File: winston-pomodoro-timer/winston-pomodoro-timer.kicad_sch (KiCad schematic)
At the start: 33 parts, among them J1 Conn_01x05_Pin, J2 Conn_01x05_Pin, J4 Conn_01x04_Pin, J5 Conn_01x06_Pin, U1 ATmega328P-A, Y1 Crystal_GND24

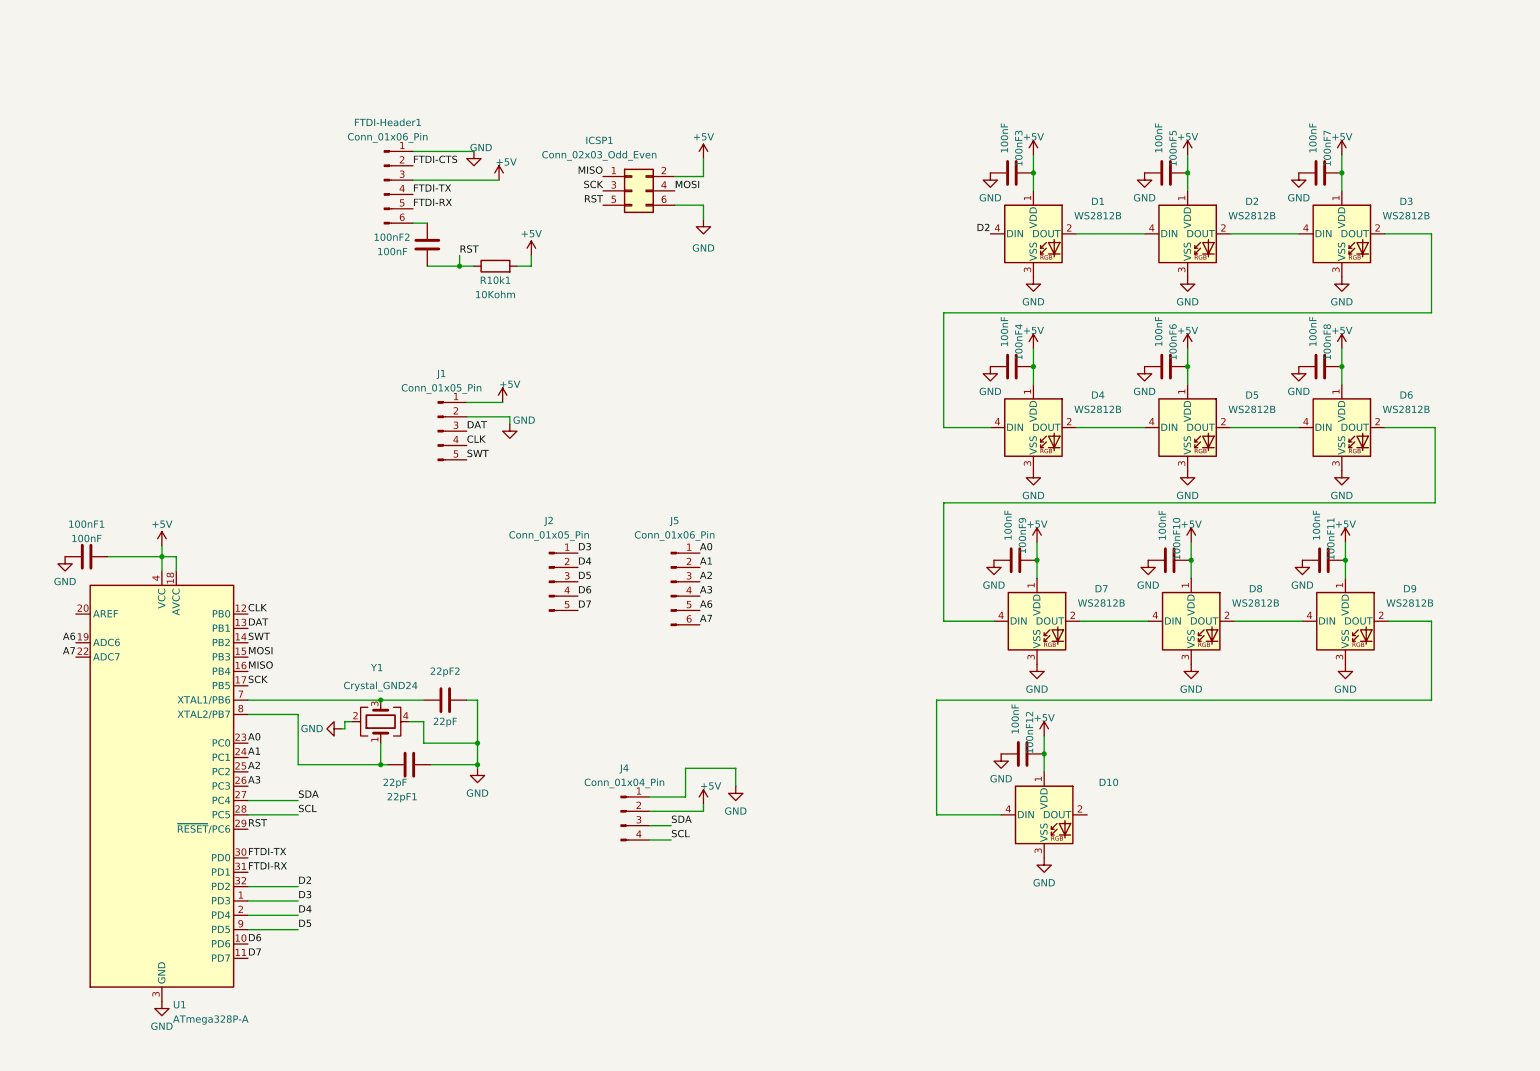
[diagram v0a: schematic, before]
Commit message: added usbc port and started battery controller
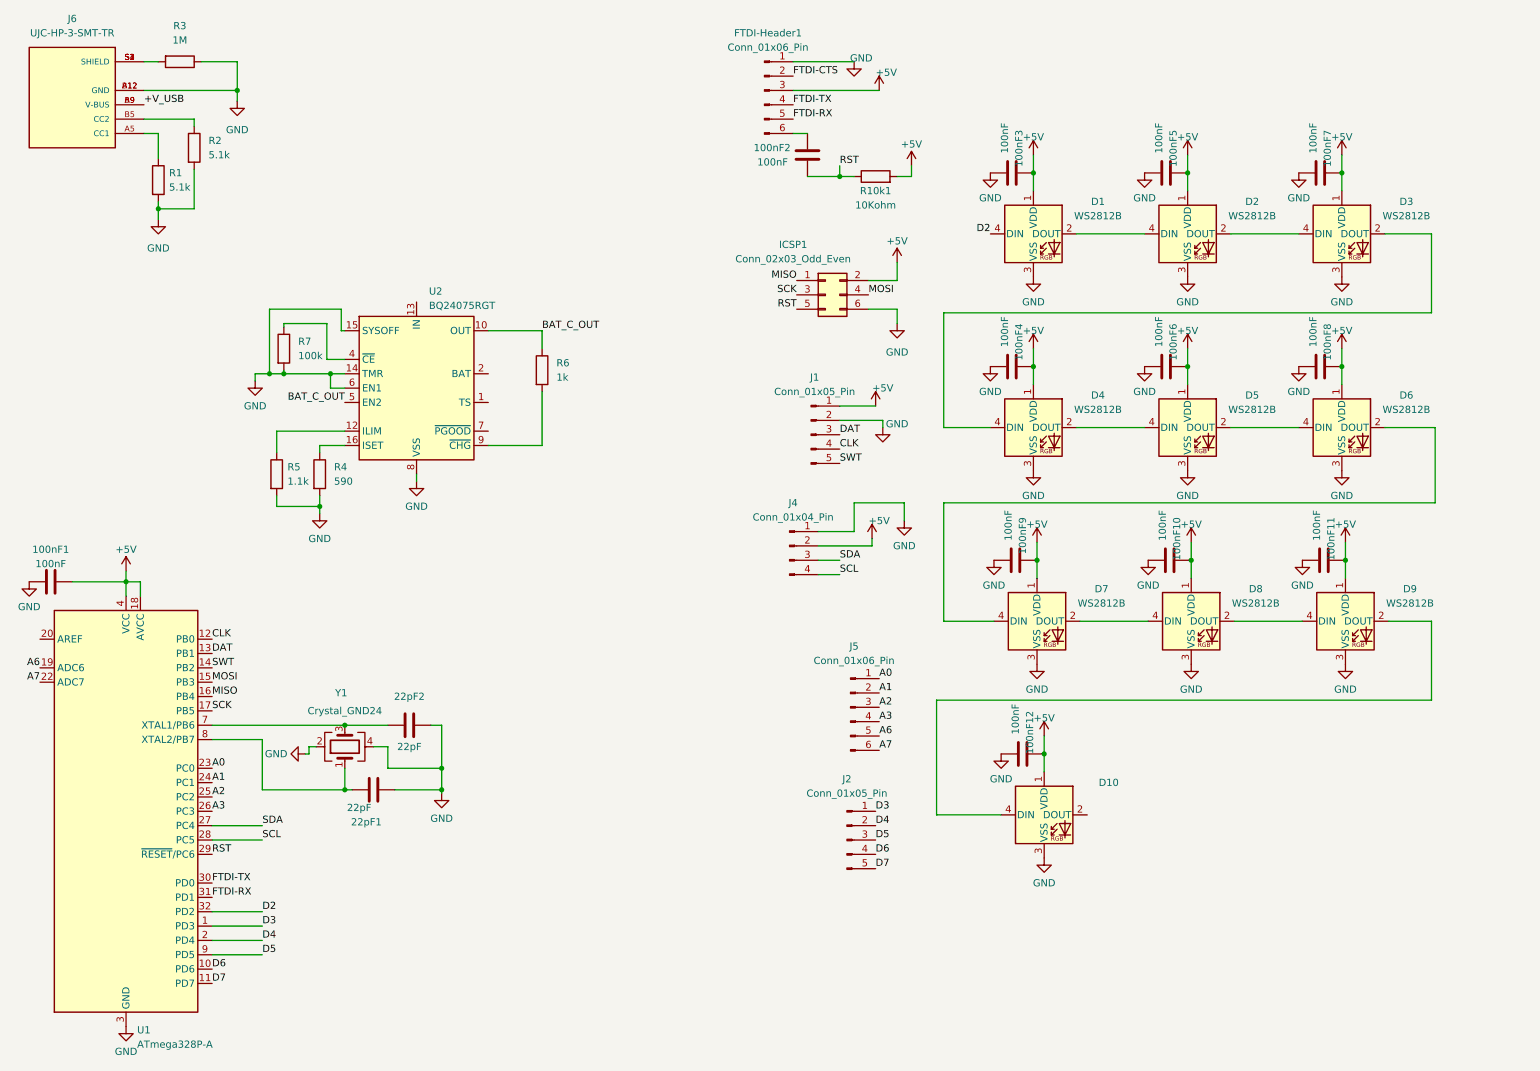
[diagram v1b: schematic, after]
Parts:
- added J6: UJC-HP-3-SMT-TR, UJC-HP-3-SMT-TR:CUI_UJC-HP-3-SMT-TR, symbol UJC-HP-3-SMT-TR:UJC-HP-3-SMT-TR
- added R1, R2: 5.1k, symbol Device:R
- added R3: 1M, symbol Device:R
- added R4: 590, symbol Device:R
- added R5: 1.1k, symbol Device:R
- added R6: 1k, symbol Device:R
- added R7: 100k, symbol Device:R
- added U2: BQ24075RGT, Package_DFN_QFN:VQFN-16-1EP_3x3mm_P0.5mm_EP1.6x1.6mm, symbol Battery_Management:BQ24075RGT
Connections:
- net GND: now also J6.A12 (GND), J6.B12 (GND), R1.2, R2.2, R3.1, R4.2, R5.2, R7.2, U2.14 (TMR), U2.15 (SYSOFF), U2.17 (VSS), U2.6 (EN1), U2.8 (VSS)
- new net: J6.S1 (SHIELD), J6.S2 (SHIELD), J6.S3 (SHIELD), J6.S4 (SHIELD), R3.2
- new net: R5.1, U2.12 (ILIM)
- new net: R4.1, U2.16 (ISET)
- new net: U2.2 (BAT), U2.3 (BAT)
- new net: R7.1, U2.4 (~{CE})
- new net: R6.2, U2.9 (~{CHG})
- new net: J6.A5 (CC1), R1.1
- new net: J6.B5 (CC2), R2.1
- new net +V_USB: J6.A9 (V-BUS), J6.B9 (V-BUS)
- new net BAT_C_OUT: R6.1, U2.10 (OUT), U2.11 (OUT), U2.5 (EN2)
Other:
- moved on the sheet: 100nF1, 100nF2, 22pF1, 22pF2, FTDI-Header1, ICSP1, J1, J2, J4, J5, R10k1, U1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

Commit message: finished layout and routing
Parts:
- added C1, C2: 10uF, Capacitor_SMD:C_0603_1608Metric, symbol Device:C
- added C3: 100uF, Capacitor_SMD:C_0805_2012Metric, symbol Device:C
- added C4: 22uF, Capacitor_SMD:C_0603_1608Metric, symbol Device:C
- added J3: Battery_Conn, Connector_PinSocket_2.00mm:PinSocket_1x02_P2.00mm_Vertical, symbol Connector:Conn_01x02_Pin
- added L1: 6.8uH, Inductor_SMD:L_Bourns-SRN4018, symbol Device:L
- added R10: 2.2M, Resistor_SMD:R_0603_1608Metric, symbol Device:R
- added R11: 390K, Resistor_SMD:R_0603_1608Metric, symbol Device:R
- added R12: 1.8M, Capacitor_SMD:C_0603_1608Metric, symbol Device:R
- added R13, R9: 200K, Resistor_SMD:R_0603_1608Metric, symbol Device:R
- added R8: 10k, Resistor_SMD:R_0603_1608Metric, symbol Device:R
- added SW2: SW_SPDT, Button_Switch_THT:SW_Slide_1P2T_CK_OS102011MS2Q, symbol Switch:SW_SPDT
- added U3: TPS61092RSAR, TPS61092RSAR:CONV_TPS61092RSAR, symbol TPS61092RSAR:TPS61092RSAR
- 100nF1, 100nF10, 100nF11, 100nF12, 100nF2, 100nF3, 100nF4, 100nF5, 100nF6, 100nF7, 100nF8, 100nF9, 22pF1, 22pF2: footprint Capacitor_SMD:C_0805_2012Metric_Pad1.18x1.45mm_HandSolder -> Capacitor_SMD:C_0603_1608Metric
- R1, R2, R3, R4, R5, R6, R7: footprint (none) -> Resistor_SMD:R_0603_1608Metric
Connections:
- net +5V: now also C3.1, R12.1, U3.1 (VOUT), U3.15 (VOUT), U3.16 (VOUT)
- net +V_USB: now also U2.13 (IN), C4.1
- net GND: now also C1.2, C2.2, C3.2, C4.2, J3.2 (Pin_2), R11.2, R13.2, R8.2, SW2.3 (C), U3.10 (SYNC), U3.12 (LBO), U3.13 (GND), U3.17 (PGND), U3.5 (PGND), U3.6 (PGND), U3.7 (PGND)
- net at U2.1 (TS): now also R8.1
- net +V_BAT: now reaches U2.2 (BAT), U2.3 (BAT)
- net +V_BAT: now also C1.1, J3.1 (Pin_1)
- net BAT_C_OUT renamed BAT_V_OUT
- net BAT_V_OUT: now also C2.1, L1.1, R10.1, SW2.1 (A), U3.8 (VBAT)
- new net: R10.2, R11.1, U3.9 (LBI)
- new net: R13.1, R9.2, U3.14 (FB)
- new net: L1.2, U3.3 (SW), U3.4 (SW)
- new net: R12.2, R9.1
- new net Boost_EN: SW2.2 (B), U3.11 (EN)
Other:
- note added: "Enable Boost"
- note added: "Power Switch"
- note added: "R10 and R11 disconnect the battery from the system when it drops below 3.35v >>Check voltage range of Winston's battery"
- note added: "Shutdown Boost"
- moved on the sheet: 22pF1, 22pF2, J2, J4, J5, R1, R2, R4, R5, R6, R7, U2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

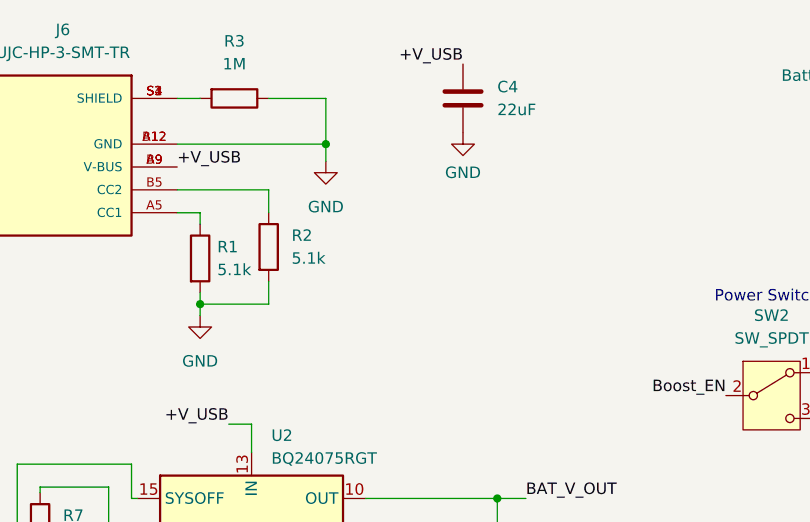
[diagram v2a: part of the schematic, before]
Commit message: added battery override jumpers
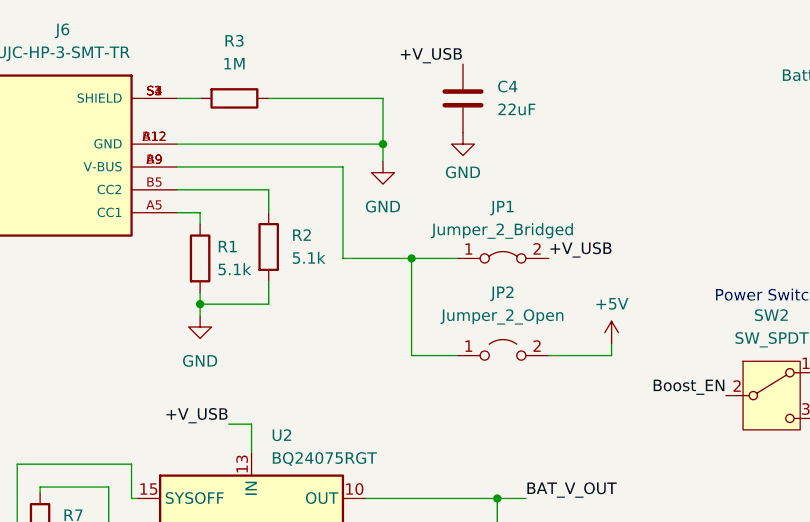
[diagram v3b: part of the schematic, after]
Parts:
- added JP1: Jumper_2_Bridged, Jumper:SolderJumper-2_P1.3mm_Bridged2Bar_RoundedPad1.0x1.5mm, symbol Jumper:Jumper_2_Bridged
- added JP2: Jumper_2_Open, Jumper:SolderJumper-2_P1.3mm_Open_RoundedPad1.0x1.5mm, symbol Jumper:Jumper_2_Open
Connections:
- net +5V: now also JP2.2 (B)
- net +V_USB: now also JP1.2 (B); no longer J6.A9 (V-BUS), J6.B9 (V-BUS)
- new net: J6.A9 (V-BUS), J6.B9 (V-BUS), JP1.1 (A), JP2.1 (A)
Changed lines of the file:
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@@
   (junction (at 19.685 74.295) (diameter 0) (color 0 0 0 0)
   )
+  (junction (at 60.96 40.005) (diameter 0) (color 0 0 0 0)
+  )
   (junction (at 17.145 74.295) (diameter 0) (color 0 0 0 0)
   )
+  (junction (at 57.785 27.305) (diameter 0) (color 0 0 0 0)
+  )
   (junction (at 247.015 41.91) (diameter 0) (color 0 0 0 0)
   )
@@
   (junction (at 194.31 144.78) (diameter 0) (color 0 0 0 0)
   )
-  (junction (at 51.435 27.305) (diameter 0) (color 0 0 0 0)
-  )
   (junction (at 153.67 171.45) (diameter 0) (color 0 0 0 0)
   )
@@
     (stroke (width 0) (type default))
   )
-  (wire (pts (xy 34.925 27.305) (xy 51.435 27.305))
+  (wire (pts (xy 34.925 27.305) (xy 57.785 27.305))
     (stroke (width 0) (type default))
   )
@@
     (stroke (width 0) (type default))
   )
-  (wire (pts (xy 51.435 27.305) (xy 51.435 29.21))
+  (wire (pts (xy 57.785 27.305) (xy 57.785 29.21))
     (stroke (width 0) (type default))
   )
@@
     (stroke (width 0) (type default))
   )
+  (wire (pts (xy 83.185 50.8) (xy 83.185 49.53))
+    (stroke (width 0) (type default))
+  )
   (wire (pts (xy 193.04 110.49) (xy 193.04 113.665))
     (stroke (width 0) (type default))
@@
     (stroke (width 0) (type default))
   )
+  (wire (pts (xy 53.34 29.845) (xy 53.34 40.005))
+    (stroke (width 0) (type default))
+  )
   (wire (pts (xy 162.56 181.61) (xy 162.56 182.88))
     (stroke (width 0) (type default))
@@
     (stroke (width 0) (type default))
   )
+  (wire (pts (xy 60.96 40.005) (xy 66.04 40.005))
+    (stroke (width 0) (type default))
+  )
   (wire (pts (xy 27.94 74.295) (xy 30.48 74.295))
     (stroke (width 0) (type default))
@@
     (stroke (width 0) (type default))
   )
-  (wire (pts (xy 51.435 22.225) (xy 51.435 27.305))
+  (wire (pts (xy 57.785 22.225) (xy 57.785 27.305))
     (stroke (width 0) (type default))
   )
@@
     (stroke (width 0) (type default))
   )
+  (wire (pts (xy 76.2 50.8) (xy 83.185 50.8))
+    (stroke (width 0) (type default))
+  )
   (wire (pts (xy 255.27 121.285) (xy 262.89 121.285))
     (stroke (width 0) (type default))
@@
     (stroke (width 0) (type default))
   )
-  (wire (pts (xy 45.085 22.225) (xy 51.435 22.225))
+  (wire (pts (xy 45.085 22.225) (xy 57.785 22.225))
     (stroke (width 0) (type default))
   )
@@
     (stroke (width 0) (type default))
   )
+  (wire (pts (xy 60.96 50.8) (xy 60.96 40.005))
+    (stroke (width 0) (type default))
+  )
   (wire (pts (xy 29.845 66.675) (xy 29.845 62.865))
     (stroke (width 0) (type default))
@@
     (stroke (width 0) (type default))
   )
+  (wire (pts (xy 66.04 50.8) (xy 60.96 50.8))
+    (stroke (width 0) (type default))
+  )
   (wire (pts (xy 150.495 180.34) (xy 150.495 182.88))
     (stroke (width 0) (type default))
@@
     (stroke (width 0) (type default))
   )
+  (wire (pts (xy 53.34 40.005) (xy 60.96 40.005))
+    (stroke (width 0) (type default))
+  )
   (wire (pts (xy 43.18 61.595) (xy 43.18 58.42))
     (stroke (width 0) (type default))
@@
     (stroke (width 0) (type default))
   )
+  (wire (pts (xy 34.925 29.845) (xy 53.34 29.845))
+    (stroke (width 0) (type default))
+  )
   (wire (pts (xy 14.605 74.295) (xy 14.605 75.565))
     (stroke (width 0) (type default))
@@
     (effects (font (size 1.27 1.27)) (justify left bottom))
   )
-  (label "+V_USB" (at 34.925 29.845 0) (fields_autoplaced)
+  (label "+V_USB" (at 76.2 40.005 0) (fields_autoplaced)
     (effects (font (size 1.27 1.27)) (justify left bottom))
   )
@@
     )
   )
+  (symbol (lib_id "Jumper:Jumper_2_Open") (at 71.12 50.8 0) (unit 1)
+    (in_bom yes) (on_board yes) (dnp no) (fields_autoplaced)
+    (property "Reference" "JP2" (at 71.12 43.815 0)
+      (effects (font (size 1.27 1.27)))
+    )
+    (property "Value" "Jumper_2_Open" (at 71.12 46.355 0)
+      (effects (font (size 1.27 1.27)))
+    )
+    (property "Footprint" "Jumper:SolderJumper-2_P1.3mm_Open_RoundedPad1.0x1.5mm" (at 71.12 50.8 0)
+      (effects (font (size 1.27 1.27)) hide)
+    )
+    (property "Datasheet" "~" (at 71.12 50.8 0)
+      (effects (font (size 1.27 1.27)) hide)
+    )
+    (pin "2")
+    (pin "1")
+    (instances
+      (project "winston-pomodoro-timer"
+        (path "/095f7656-1187-413c-b258-1af41f7d9209"
+          (reference "JP2") (unit 1)
+        )
+      )
+    )
+  )
   (symbol (lib_id "LED:WS2812B") (at 192.405 52.705 0) (unit 1)
     (in_bom yes) (on_board yes) (dnp no)
@@
     )
   )
+  (symbol (lib_id "power:+5V") (at 83.185 49.53 0) (unit 1)
+    (in_bom yes) (on_board yes) (dnp no) (fields_autoplaced)
+    (property "Reference" "#PWR054" (at 83.185 53.34 0)
+      (effects (font (size 1.27 1.27)) hide)
+    )
+    (property "Value" "+5V" (at 83.185 45.085 0)
+      (effects (font (size 1.27 1.27)))
+    )
+    (property "Footprint" "" (at 83.185 49.53 0)
+      (effects (font (size 1.27 1.27)) hide)
+    )
+    (property "Datasheet" "" (at 83.185 49.53 0)
+      (effects (font (size 1.27 1.27)) hide)
+    )
+    (pin "1")
+    (instances
+      (project "winston-pomodoro-timer"
+        (path "/095f7656-1187-413c-b258-1af41f7d9209"
+          (reference "#PWR054") (unit 1)
+        )
+      )
+    )
+  )
   (symbol (lib_id "Device:C") (at 190.5 144.78 90) (unit 1)
     (in_bom yes) (on_board yes) (dnp no)
@@
     )
   )
+  (symbol (lib_id "Jumper:Jumper_2_Bridged") (at 71.12 40.005 0) (unit 1)
+    (in_bom yes) (on_board yes) (dnp no) (fields_autoplaced)
+    (property "Reference" "JP1" (at 71.12 34.29 0)
+      (effects (font (size 1.27 1.27)))
+    )
+    (property "Value" "Jumper_2_Bridged" (at 71.12 36.83 0)
+      (effects (font (size 1.27 1.27)))
+    )
+    (property "Footprint" "Jumper:SolderJumper-2_P1.3mm_Bridged2Bar_RoundedPad1.0x1.5mm" (at 71.12 40.005 0)
+      (effects (font (size 1.27 1.27)) hide)
+    )
+    (property "Datasheet" "~" (at 71.12 40.005 0)
+      (effects (font (size 1.27 1.27)) hide)
+    )
+    (pin "2")
+    (pin "1")
+    (instances
+      (project "winston-pomodoro-timer"
+        (path "/095f7656-1187-413c-b258-1af41f7d9209"
+          (reference "JP1") (unit 1)
+        )
+      )
+    )
+  )
   (symbol (lib_id "power:GND") (at 185.42 110.49 0) (mirror y) (unit 1)
     (in_bom yes) (on_board yes) (dnp no)
@@
     )
   )
-  (symbol (lib_id "power:GND") (at 51.435 29.21 0) (unit 1)
+  (symbol (lib_id "power:GND") (at 57.785 29.21 0) (unit 1)
     (in_bom yes) (on_board yes) (dnp no) (fields_autoplaced)
-    (property "Reference" "#PWR047" (at 51.435 35.56 0)
+    (property "Reference" "#PWR047" (at 57.785 35.56 0)
       (effects (font (size 1.27 1.27)) hide)
     )
-    (property "Value" "GND" (at 51.435 34.29 0)
+    (property "Value" "GND" (at 57.785 34.29 0)
       (effects (font (size 1.27 1.27)))
     )
-    (property "Footprint" "" (at 51.435 29.21 0)
+    (property "Footprint" "" (at 57.785 29.21 0)
       (effects (font (size 1.27 1.27)) hide)
     )
-    (property "Datasheet" "" (at 51.435 29.21 0)
+    (property "Datasheet" "" (at 57.785 29.21 0)
       (effects (font (size 1.27 1.27)) hide)
     )
